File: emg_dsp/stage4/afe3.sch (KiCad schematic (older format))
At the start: 68 parts, among them U49 LP2985-40, U50 TPS73025, U51 BAT54S, U52 78250M, U53 MAX253, U54 BAT54S, U55 BAT54S, U56 BAT54S, U57 BAT54S, U58 BAT54S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

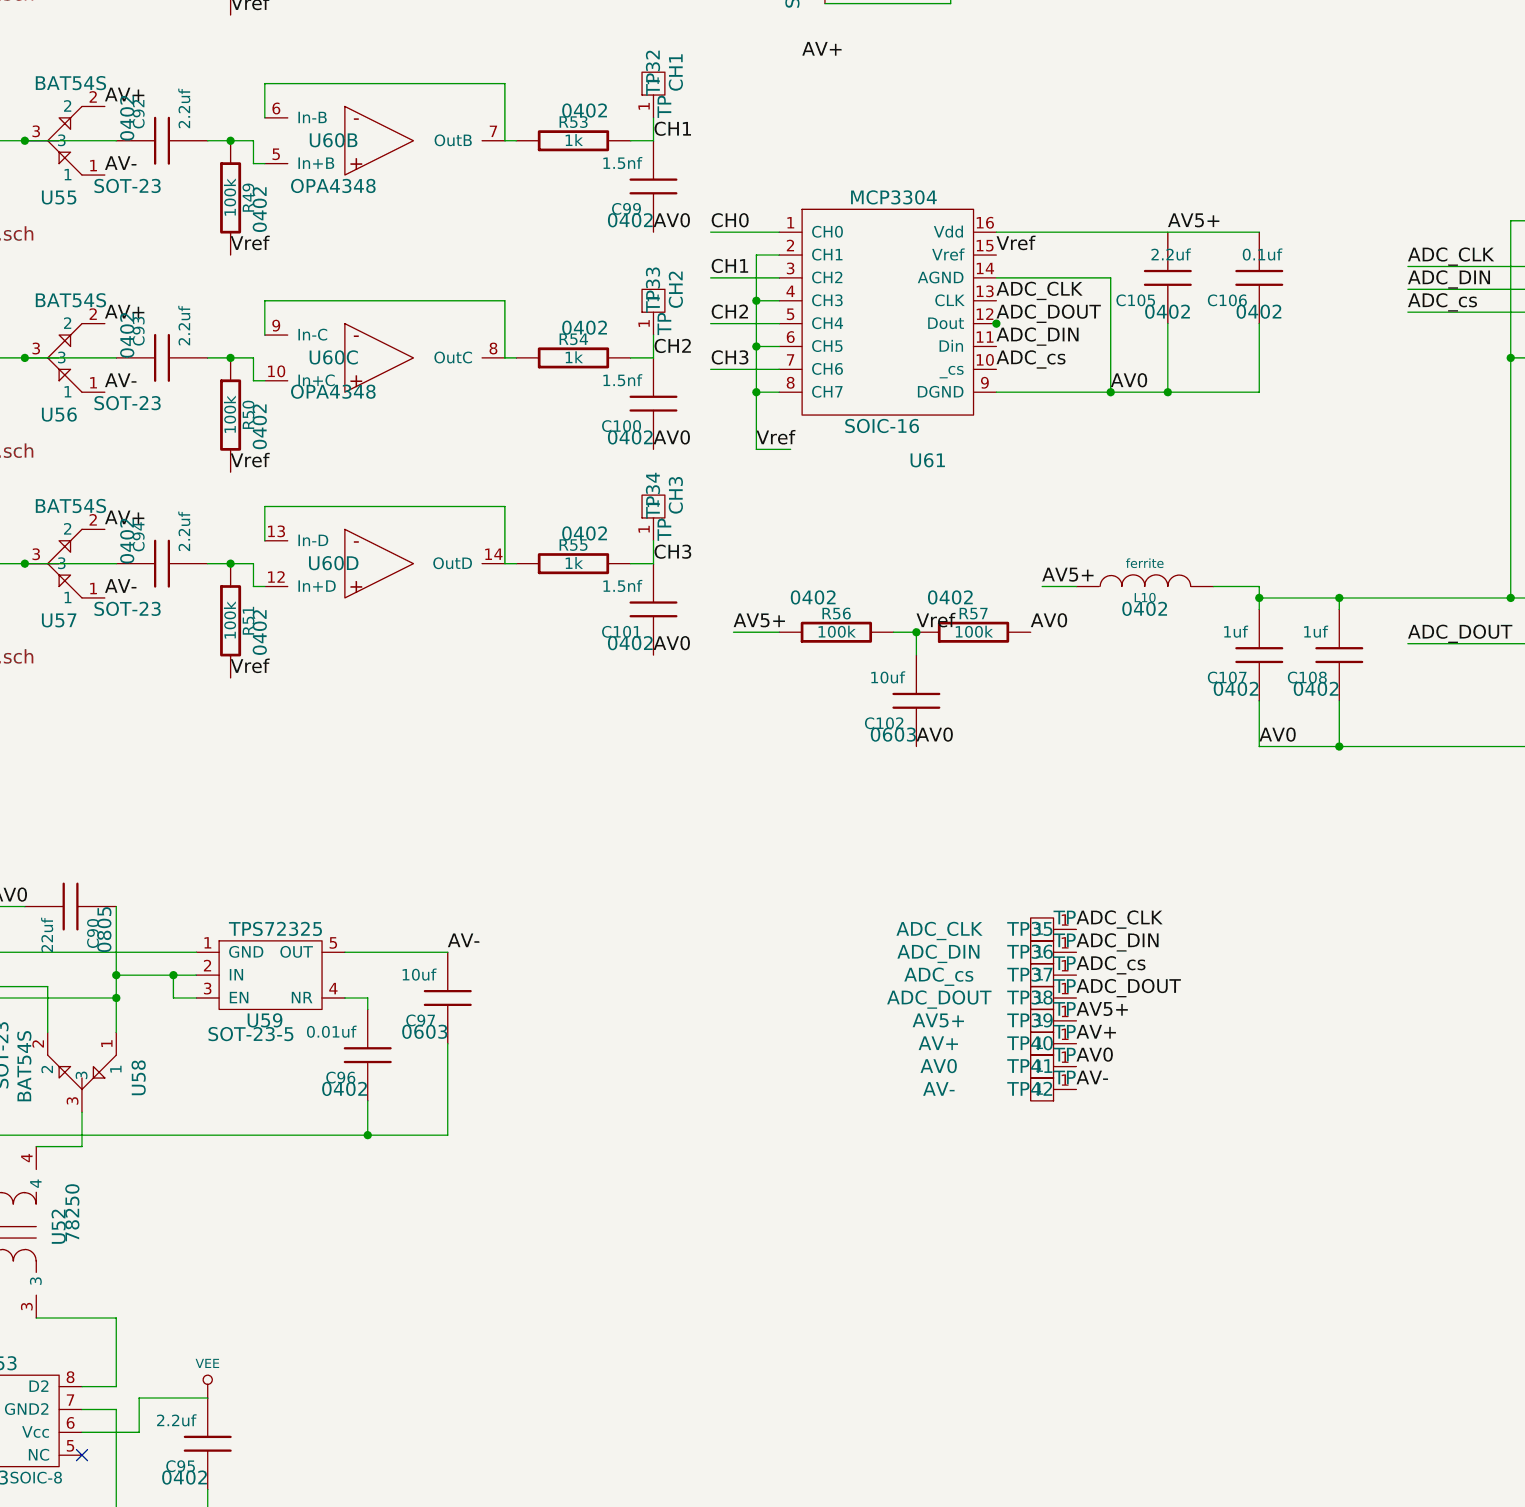
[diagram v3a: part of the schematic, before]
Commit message: cleaned up the power supplies.  not sure what i was thinking before - 2.85V should be fine for Vdd.
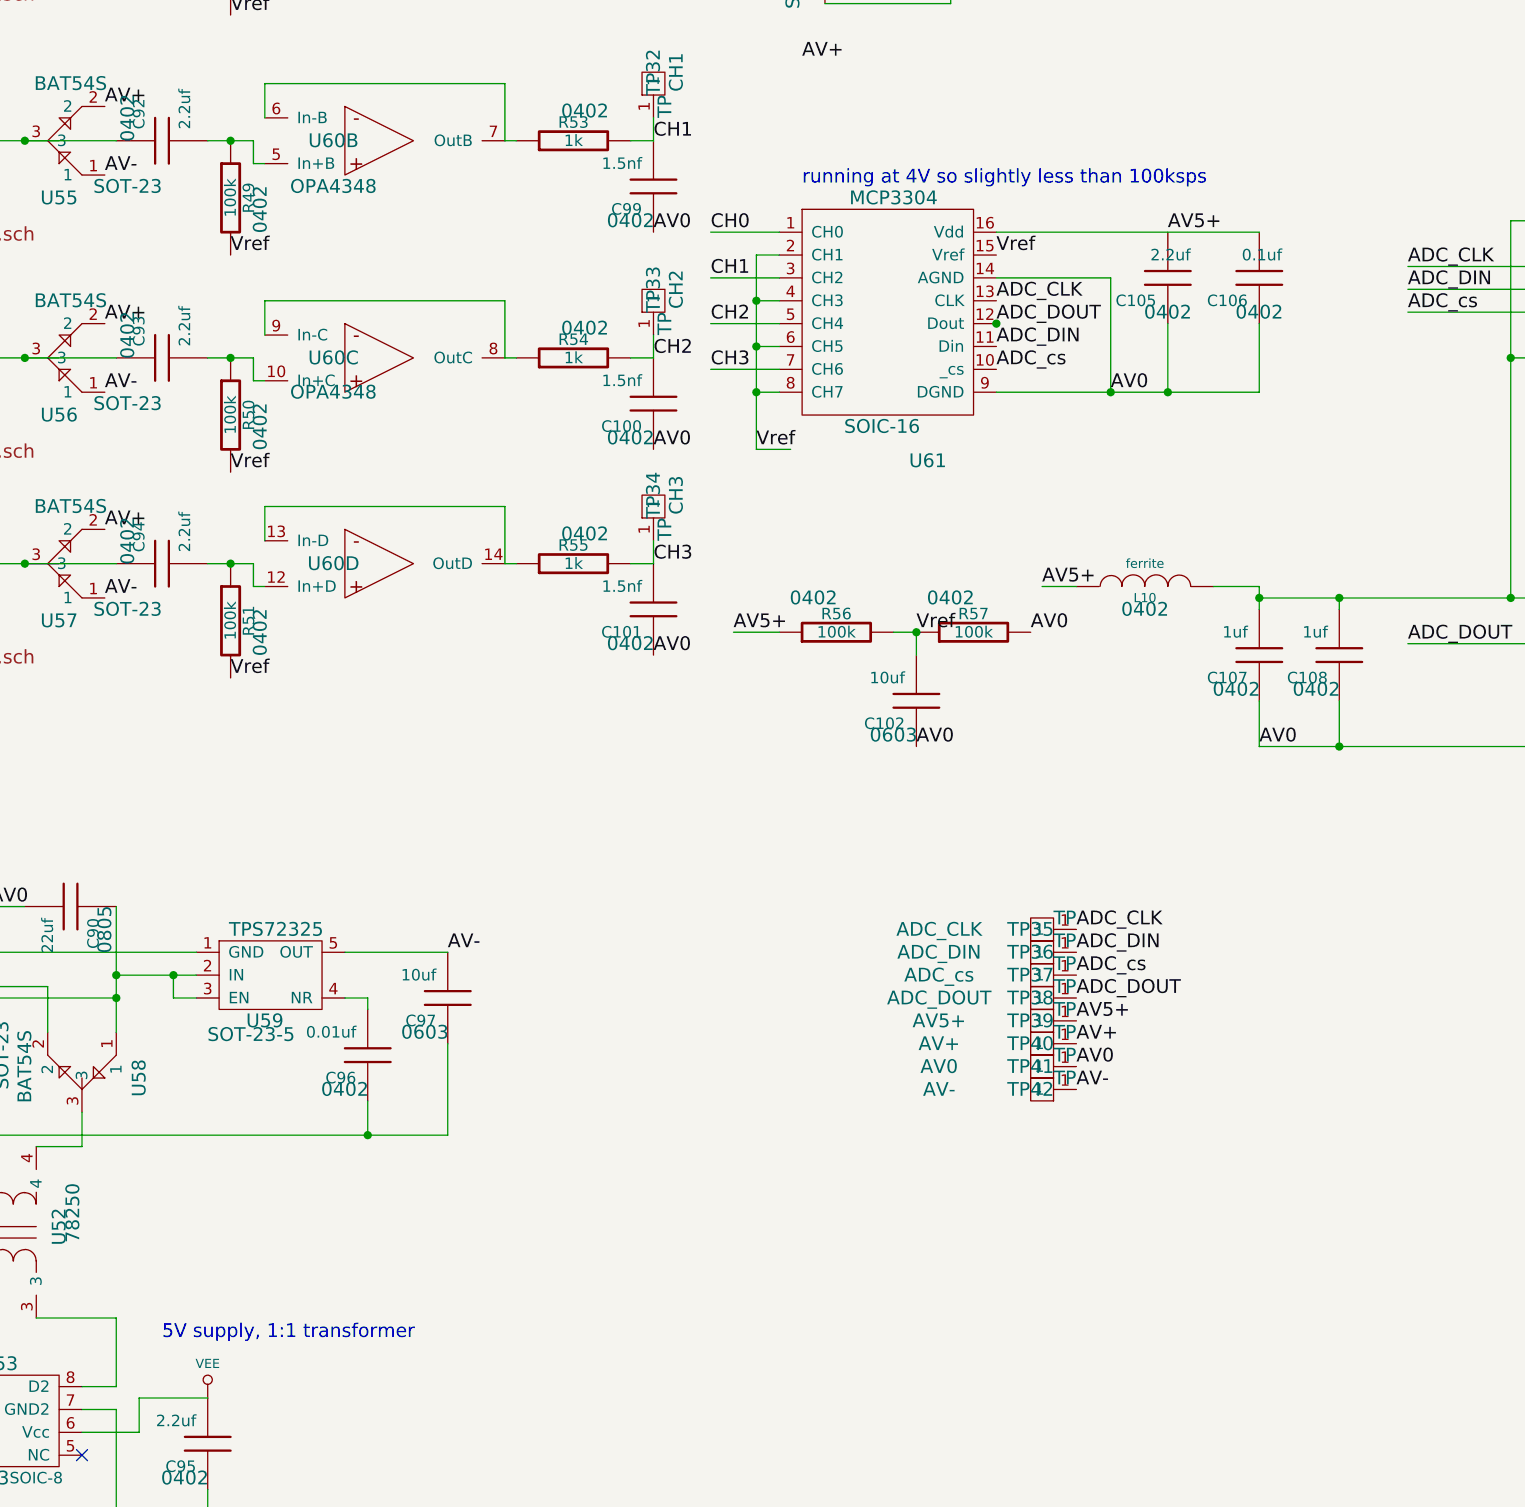
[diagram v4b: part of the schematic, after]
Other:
- note added: "5V supply, 1:1 transformer"
- note added: "running at 4V so slightly less than 100ksps"
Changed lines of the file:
@@
-EESchema Schematic File Version 2  date Wed 17 Feb 2010 06:02:14 PM EST
+EESchema Schematic File Version 2  date Wed 17 Feb 2010 07:09:19 PM EST
 LIBS:power,device,emg_sym,/home/tlh24/svn/myopen/emg_dsp/lib/linear,./stage4.cache
 EELAYER 24  0
@@
 Sheet 7 44
 Title ""
-Date "17 feb 2010"
+Date "18 feb 2010"
 Rev ""
 Comp ""
@@
 Comment4 ""
 $EndDescr
+Text Notes 6950 2700 0    60   ~ 0
+running at 4V so slightly less than 100ksps
+Text Notes 4150 7750 0    60   ~ 0
+5V supply, 1:1 transformer
 Connection ~ 9300 5150
 Connection ~ 10150 5150
@@
 note: changed to 4V to give the LDO more headroom
 $Comp
-L GND #PWR0210
+L GND #PWR203
 U 1 1 4B6B021D
 P 2000 7850
-F 0 "#PWR0210" H 2000 7850 30  0001 C CNN
+F 0 "#PWR203" H 2000 7850 30  0001 C CNN
 F 1 "GND" H 2000 7780 30  0001 C CNN
 	1    2000 7850
@@
 min 3V supply
 $Comp
-L GND #PWR0211
+L GND #PWR205
 U 1 1 4B6A0B2D
 P 3950 8550
-F 0 "#PWR0211" H 3950 8550 30  0001 C CNN
+F 0 "#PWR205" H 3950 8550 30  0001 C CNN
 F 1 "GND" H 3950 8480 30  0001 C CNN
 	1    3950 8550
@@
 $EndComp
 $Comp
-L VEE #PWR203
+L VEE #PWR204
 U 1 1 4B6A0B22
 P 2550 8150
-F 0 "#PWR203" H 2550 8350 40  0001 C CNN
+F 0 "#PWR204" H 2550 8350 40  0001 C CNN
 F 1 "VEE" H 2550 8300 40  0000 C CNN
 	1    2550 8150
@@
 $EndComp
 $Comp
-L VEE #PWR205
+L VEE #PWR206
 U 1 1 4B6A0B1D
 P 4350 8000
-F 0 "#PWR205" H 4350 8200 40  0001 C CNN
+F 0 "#PWR206" H 4350 8200 40  0001 C CNN
 F 1 "VEE" H 4350 8150 40  0000 C CNN
 	1    4350 8000

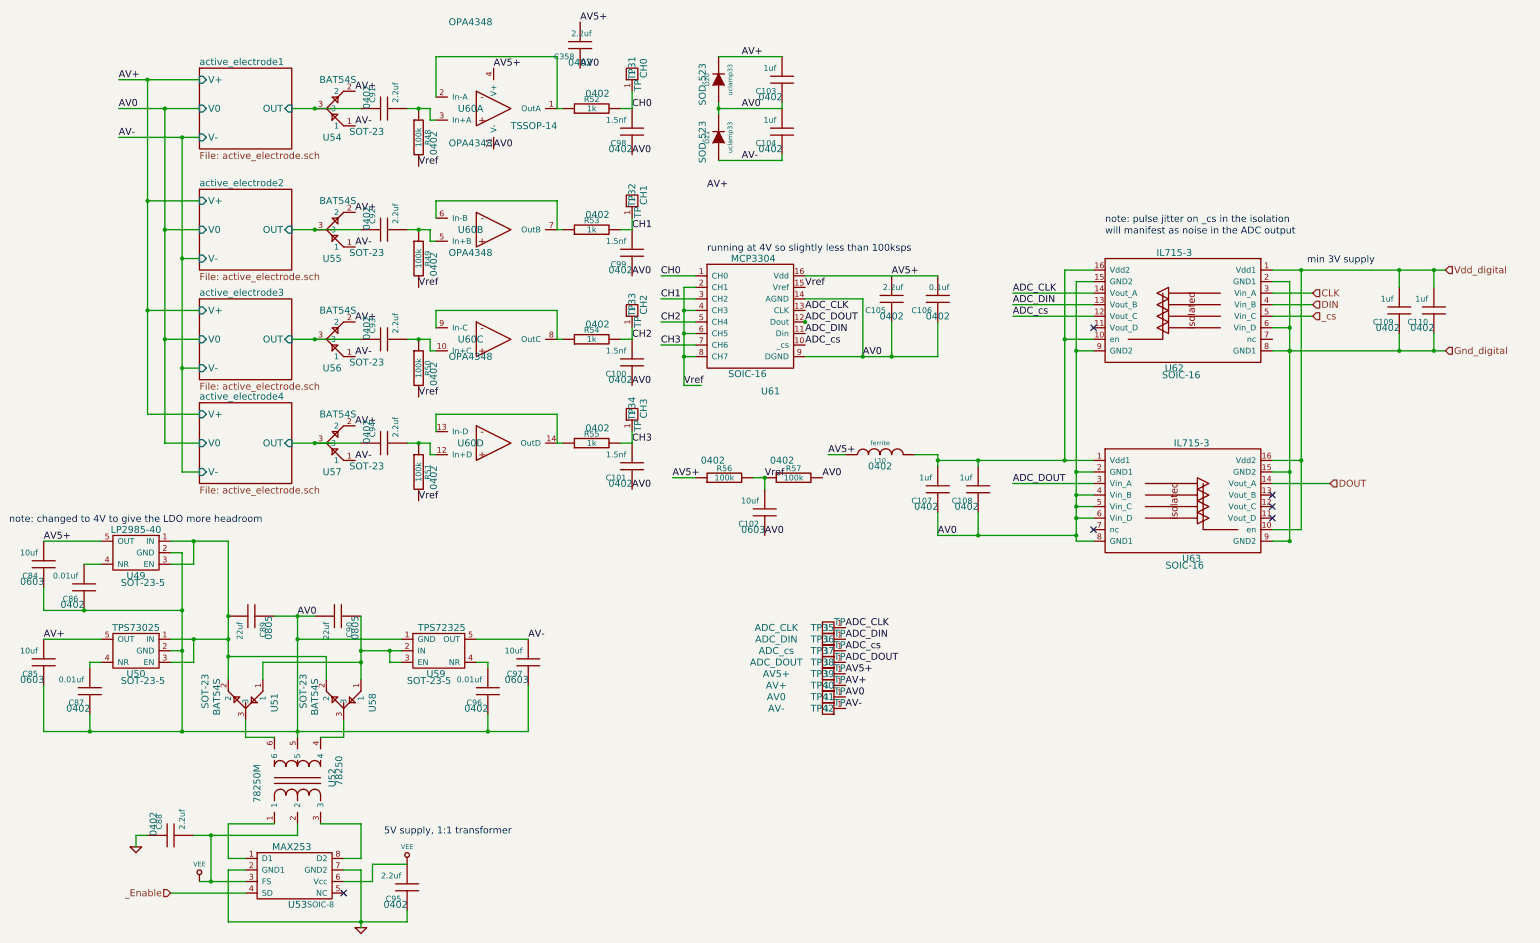
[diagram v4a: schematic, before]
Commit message: changed the meg isolator to something that will work at 2.7V
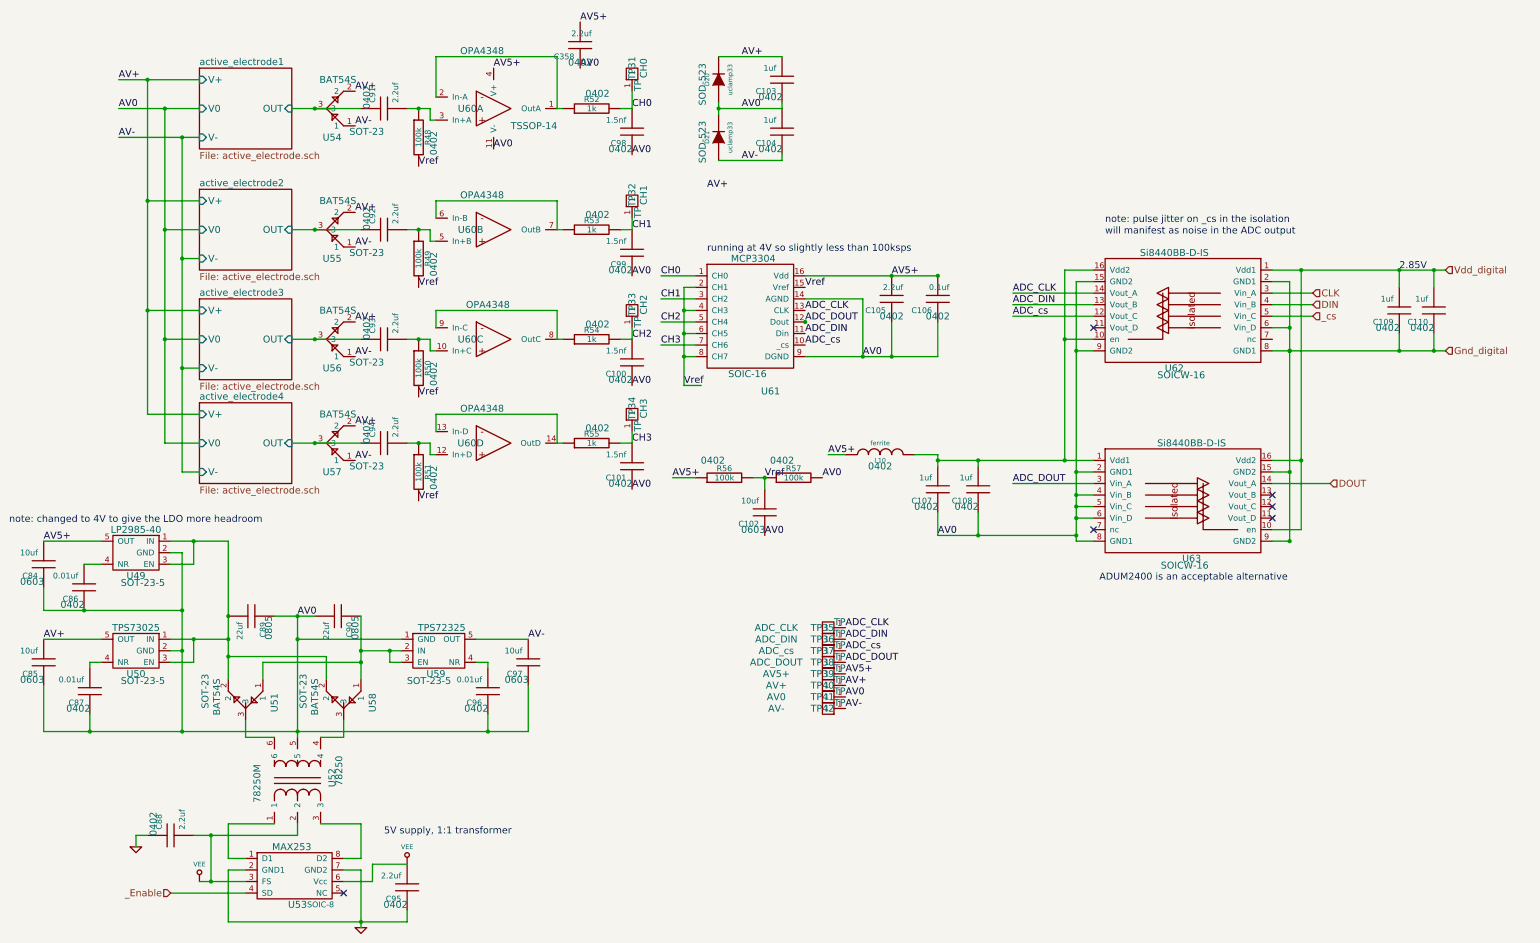
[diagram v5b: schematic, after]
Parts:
- U62, U63: value IL715-3 -> Si8440BB-D-IS; footprint SOIC-16 -> SOICW-16
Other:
- note added: "2.85V"
- note added: "ADUM2400 is an acceptable alternative"
- note removed: "min 3V supply"
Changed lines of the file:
@@
-EESchema Schematic File Version 2  date Wed 17 Feb 2010 07:09:19 PM EST
+EESchema Schematic File Version 2  date Thu 18 Feb 2010 10:54:00 AM EST
 LIBS:power,device,emg_sym,/home/tlh24/svn/myopen/emg_dsp/lib/linear,./stage4.cache
 EELAYER 24  0
@@
 Comment4 ""
 $EndDescr
+Connection ~ 8950 2900
+Connection ~ 8550 2900
+Text Notes 12950 2850 0    60   ~ 0
+2.85V
+Text Notes 10350 5550 0    60   ~ 0
+ADUM2400 is an acceptable alternative
 Text Notes 6950 2700 0    60   ~ 0
 running at 4V so slightly less than 100ksps
@@
 note: changed to 4V to give the LDO more headroom
 $Comp
-L GND #PWR203
+L GND #PWR0206
 U 1 1 4B6B021D
 P 2000 7850
-F 0 "#PWR203" H 2000 7850 30  0001 C CNN
+F 0 "#PWR0206" H 2000 7850 30  0001 C CNN
 F 1 "GND" H 2000 7780 30  0001 C CNN
 	1    2000 7850
@@
 	-1   0    0    1
 $EndComp
-Text Notes 12150 2800 0    60   ~ 0
-min 3V supply
-$Comp
-L GND #PWR205
+$Comp
+L GND #PWR0207
 U 1 1 4B6A0B2D
 P 3950 8550
-F 0 "#PWR205" H 3950 8550 30  0001 C CNN
+F 0 "#PWR0207" H 3950 8550 30  0001 C CNN
 F 1 "GND" H 3950 8480 30  0001 C CNN
 	1    3950 8550
@@
 $EndComp
 $Comp
-L VEE #PWR204
+L VEE #PWR200
 U 1 1 4B6A0B22
 P 2550 8150
-F 0 "#PWR204" H 2550 8350 40  0001 C CNN
+F 0 "#PWR200" H 2550 8350 40  0001 C CNN
 F 1 "VEE" H 2550 8300 40  0000 C CNN
 	1    2550 8150
@@
 $EndComp
 $Comp
-L VEE #PWR206
+L VEE #PWR202
 U 1 1 4B6A0B1D
 P 4350 8000
-F 0 "#PWR206" H 4350 8200 40  0001 C CNN
+F 0 "#PWR202" H 4350 8200 40  0001 C CNN
 F 1 "VEE" H 4350 8150 40  0000 C CNN
 	1    4350 8000
@@
 P 11150 5050
 F 0 "U63" H 11150 4750 60  0000 C CNN
-F 1 "IL715-3" H 11150 5750 60  0000 C CNN
-F 2 "SOIC-16" H 11090 4690 60  0000 C CNN
+F 1 "Si8440BB-D-IS" H 11150 5750 60  0000 C CNN
+F 2 "SOICW-16" H 11090 4690 60  0000 C CNN
 	1    11150 5050
 	1    0    0    -1
@@
 P 11000 3400
 F 0 "U62" H 11000 3100 60  0000 C CNN
-F 1 "IL715-3" H 11000 4100 60  0000 C CNN
-F 2 "SOIC-16" H 10940 3040 60  0000 C CNN
+F 1 "Si8440BB-D-IS" H 11000 4100 60  0000 C CNN
+F 2 "SOICW-16" H 10940 3040 60  0000 C CNN
 	1    11000 3400
 	-1   0    0    -1
@@
 P 5100 4350
 F 0 "U60" H 4900 4350 60  0000 C CNN
-F 1 "OPA4348" H 4900 5100 60  0000 C CNN
+F 1 "OPA4348" H 5000 4650 60  0000 C CNN
 F 2 "TSSOP-14" H 4840 4290 60  0001 C CNN
 	4    5100 4350
@@
 P 5100 3450
 F 0 "U60" H 4900 3450 60  0000 C CNN
-F 1 "OPA4348" H 4900 4200 60  0000 C CNN
+F 1 "OPA4348" H 5050 3750 60  0000 C CNN
 F 2 "TSSOP-14" H 4840 3390 60  0001 C CNN
 	3    5100 3450
@@
 P 5100 2500
 F 0 "U60" H 4900 2500 60  0000 C CNN
-F 1 "OPA4348" H 4900 3250 60  0000 C CNN
+F 1 "OPA4348" H 5000 2800 60  0000 C CNN
 F 2 "TSSOP-14" H 4840 2440 60  0001 C CNN
 	2    5100 2500
@@
 P 5100 1450
 F 0 "U60" H 4900 1450 60  0000 C CNN
-F 1 "OPA4348" H 4900 2200 60  0000 C CNN
+F 1 "OPA4348" H 5000 1950 60  0000 C CNN
 F 2 "TSSOP-14" H 5450 1300 60  0000 C CNN
 	1    5100 1450
